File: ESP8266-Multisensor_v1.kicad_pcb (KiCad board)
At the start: 2 copper layers, 69.8 x 50 mm, 73 parts

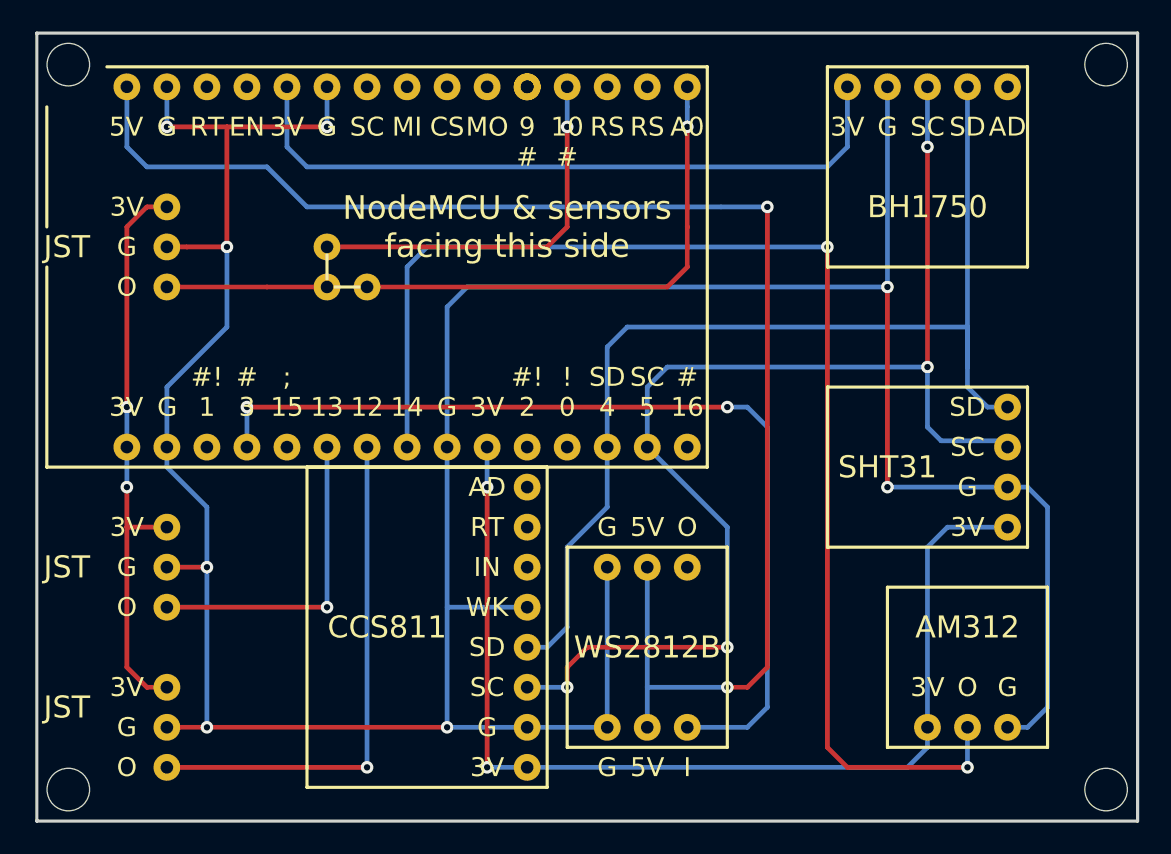
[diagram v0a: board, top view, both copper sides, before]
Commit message: PCB bugfixes
increased drill hole size and pad size
made silkscreen nicer
changed jumper to not only work with pin header but also solder bridge
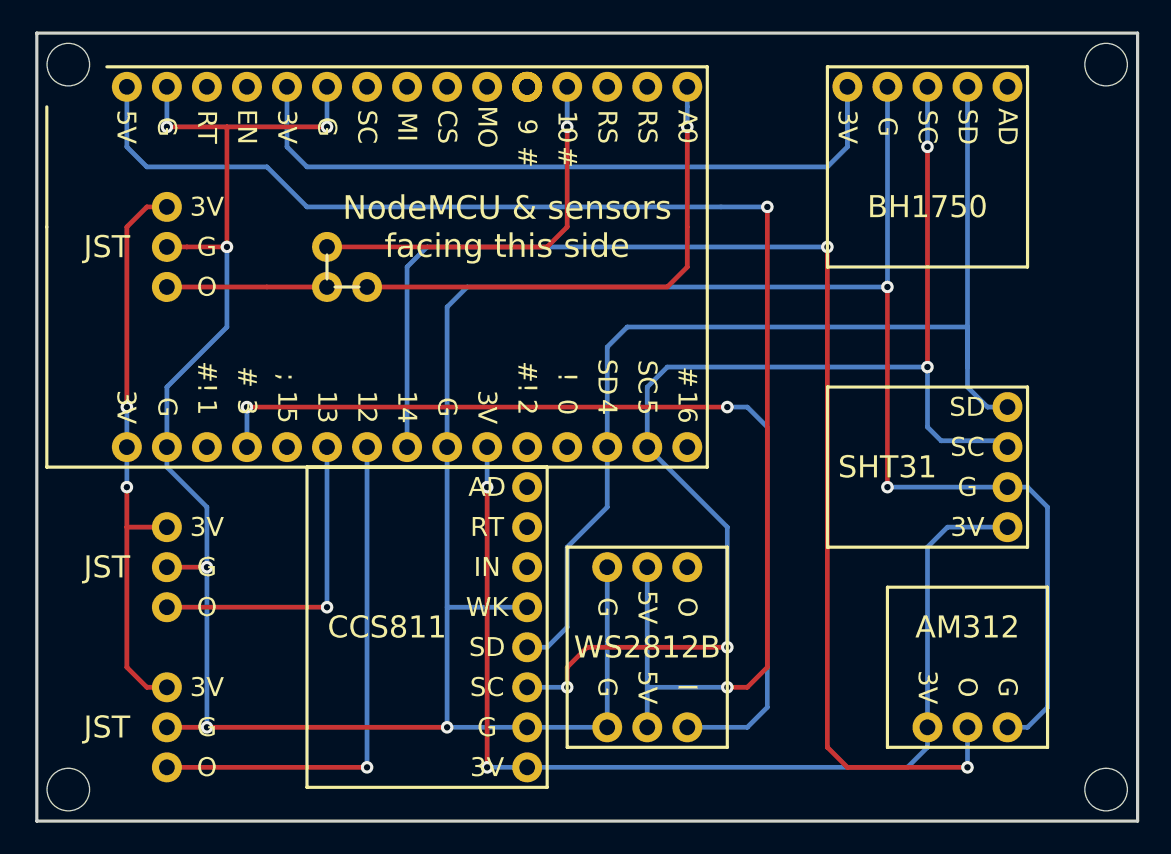
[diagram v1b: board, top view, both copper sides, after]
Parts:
- REF** (x69): value TestPoint_THTPad_D1.5mm_Drill0.8mm -> TestPoint_THTPad_D1.9mm_Drill1.0mm; footprint TestPoint:TestPoint_THTPad_D1.5mm_Drill0.8mm -> TestPoint:TestPoint_THTPad_D1.9mm_Drill1.0mm
